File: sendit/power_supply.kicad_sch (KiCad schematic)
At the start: 44 parts, among them J36 Conn_01x02, J37 Conn_01x02, J38 JUMPER, U10 TPS61040DBV, U11 AP63205WU, U9 TPS7A2033PDBVR

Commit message: power system work and layout
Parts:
- removed C35: 22pF / 50v, Capacitor_SMD:C_0603_1608Metric, symbol Device:C_Small
- removed C38: 1uF / 50v, Capacitor_SMD:C_0603_1608Metric, symbol Device:C_Small
- removed D19: MBR0530, Diode_SMD:D_SOD-123, symbol Diode:MBR0530
- removed FB3: BLM18AG121SN1D, Inductor_SMD:L_0603_1608Metric, symbol Device:FerriteBead_Small
- removed U10: TPS61040DBV, Package_TO_SOT_SMD:SOT-23-5, symbol Regulator_Switching:TPS61040DBV
- added D20: SS36, Diode_SMD:D_SMA, symbol Diode:SS36
- added U10: MT3608, Package_TO_SOT_SMD:SOT-23-6, symbol Regulator_Switching:MT3608
- C30: value 10uF / 10v -> 22uF / 10v; LCSC C19702 -> (none)
- C35: renamed from C36; value 1uF / 50v -> 22uF / 50v
- L1: footprint Inductor_SMD:L_APV_ANR252012 -> Inductor_SMD:L_TechFuse_SL0630; LCSC C5832376 -> C167223
- R53: value 1.87M -> 390K 1%; LCSC C61679 -> (none)
- R54: value 100k -> 10k 0.1%; LCSC C25803 -> (none)
- renumbered C37 to C36, C39 to C37, C40 to C38, D20 to D19, J36 to J37, J37 to J38, J38 to J39, TP17 to TP15, TP15 to TP16, TP16 to TP17
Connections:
- net +24V: now also F7.1
- net +3.3V: now also JP1.3 (B); no longer JP1.1 (A)
- net +3.3VADC: now also TP16.1
- net +5V: now also U10.4 (EN), U10.5 (IN)
- net GND: now also U10.2 (GND)
- net VEXT: now also TP15.1
- net at C31.1, C32.1, C33.1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: now also JP1.1 (A); no longer JP1.3 (B), TP16.1
- net at C35.1: now also F7.2, R53.1, D20.1 (K); no longer F7.1
- net at R53.2, R54.1: now also U10.3 (FB)
- net at L1.2: now also D20.2 (A), U10.1 (SW)
- net at C34.1, F6.2, U11.2 (EN)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: no longer TP15.1
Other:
- note added: "POWER TOPOLOGY"
- moved on the sheet: C30, C35, C37, D15, D21, F7, JP1, L1, R51, R53, R54, R55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

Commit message: big change removing the usb hub and serial chip.
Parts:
- removed D16: MBR0530, Diode_SMD:D_SOD-123, symbol Diode:MBR0530
- removed J38: Conn_01x02, Connector_PinSocket_2.54mm:PinSocket_1x02_P2.54mm_Vertical, symbol Connector_Generic:Conn_01x02
- removed J39: JUMPER, symbol Connector_Generic:Conn_01x02
- added D17: SS36, Diode_SMD:D_SMA, symbol Diode:SS36
- renumbered C28 to C20, C29 to C21, C30 to C22, C31 to C23, C32 to C24, C33 to C25, C34 to C26, C35 to C27, C36 to C28, C37 to C29, C38 to C30, D17 to D16, J37 to J38, R51 to R45, R52 to R46, R53 to R47, R54 to R48, R55 to R49, TP14 to TP16, TP15 to TP17, TP16 to TP18, TP17 to TP19, TP18 to TP20, U9 to U7, U10 to U8, U11 to U9
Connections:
- net VEXT: now also F6.1, D17.1 (K)
- net at INPUT6.1 (Pin_1): now also D17.2 (A)
- no-connect marks 4 -> 2
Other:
- moved on the sheet: D18, INPUT6, J38, R46, TP17

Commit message: first pass fully routed.
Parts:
- added D20: GREEN, LED_SMD:LED_0603_1608Metric, symbol Device:LED
- added R46: 5.1k, Resistor_SMD:R_0603_1608Metric, symbol Device:R_Small_US
- renumbered D15 to D14, D16 to D15, D17 to D16, D18 to D17, D19 to D18, D20 to D19, R45 to R44, R46 to R45, TP20 to TP21
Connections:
- net +3.3VADC: now also D20.2 (A)
- net GND: now also R46.2
- new net: D20.1 (K), R46.1
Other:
- moved on the sheet: TP18

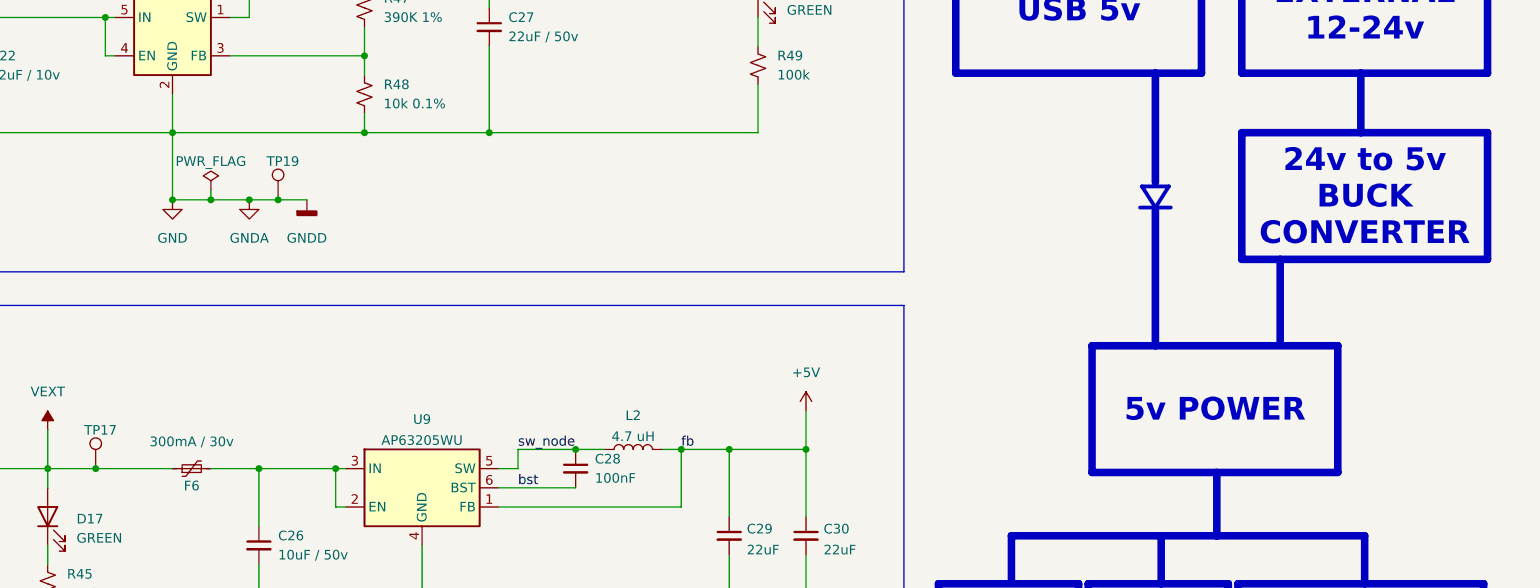
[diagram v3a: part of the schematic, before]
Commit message: beefed up the 24v to 5v circuit
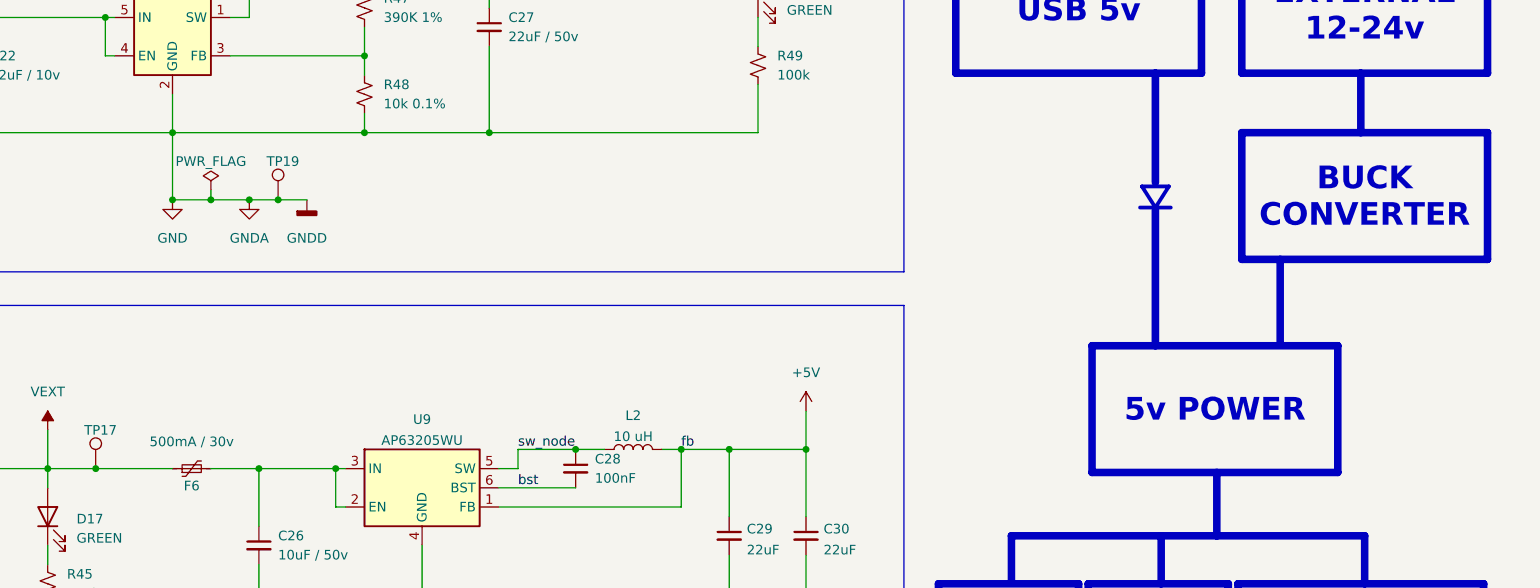
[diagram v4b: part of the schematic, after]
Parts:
- F6: value 300mA / 30v -> 500mA / 30v; footprint Fuse:Fuse_0805_2012Metric -> Fuse:Fuse_1206_3216Metric; LCSC C22378359 -> C455450
- L2: value 4.7 uH -> 10 uH; footprint Inductor_SMD:L_Neosid_SMS-ME3010 -> Inductor_SMD:L_Chilisin_BMRA00050530; LCSC C354557 -> C177248; PARTNUM CKCS3012-4.7uH/M -> FXL0530-100-M
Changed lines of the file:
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@@
 		)
 	)
-	(text_box "24v to 5v BUCK CONVERTER"
+	(text_box "BUCK CONVERTER"
 		(exclude_from_sim no)
 		(at 249.428 62.23 0)
@@
 			)
 		)
-		(property "Value" "4.7 uH"
+		(property "Value" "10 uH"
 			(at 168.91 102.4406 90)
 			(effects
@@
 			)
 		)
-		(property "Footprint" "Inductor_SMD:L_Neosid_SMS-ME3010"
+		(property "Footprint" "Inductor_SMD:L_Chilisin_BMRA00050530"
 			(at 168.91 104.14 0)
 			(effects
@@
 			)
 		)
-		(property "LCSC" "C354557"
+		(property "LCSC" "C177248"
 			(at 168.91 104.14 0)
 			(effects
@@
 			)
 		)
-		(property "PARTNUM" "CKCS3012-4.7uH/M"
+		(property "PARTNUM" "FXL0530-100-M"
 			(at 168.91 104.14 0)
 			(effects
@@
 			)
 		)
-		(property "Value" "300mA / 30v"
+		(property "Value" "500mA / 30v"
 			(at 110.49 103.124 90)
 			(effects
@@
 			)
 		)
-		(property "Footprint" "Fuse:Fuse_0805_2012Metric"
+		(property "Footprint" "Fuse:Fuse_1206_3216Metric"
 			(at 115.57 105.41 0)
 			(effects
@@
 			)
 		)
-		(property "LCSC" "C22378359"
+		(property "LCSC" "C455450"
 			(at 110.49 106.68 90)
 			(effects

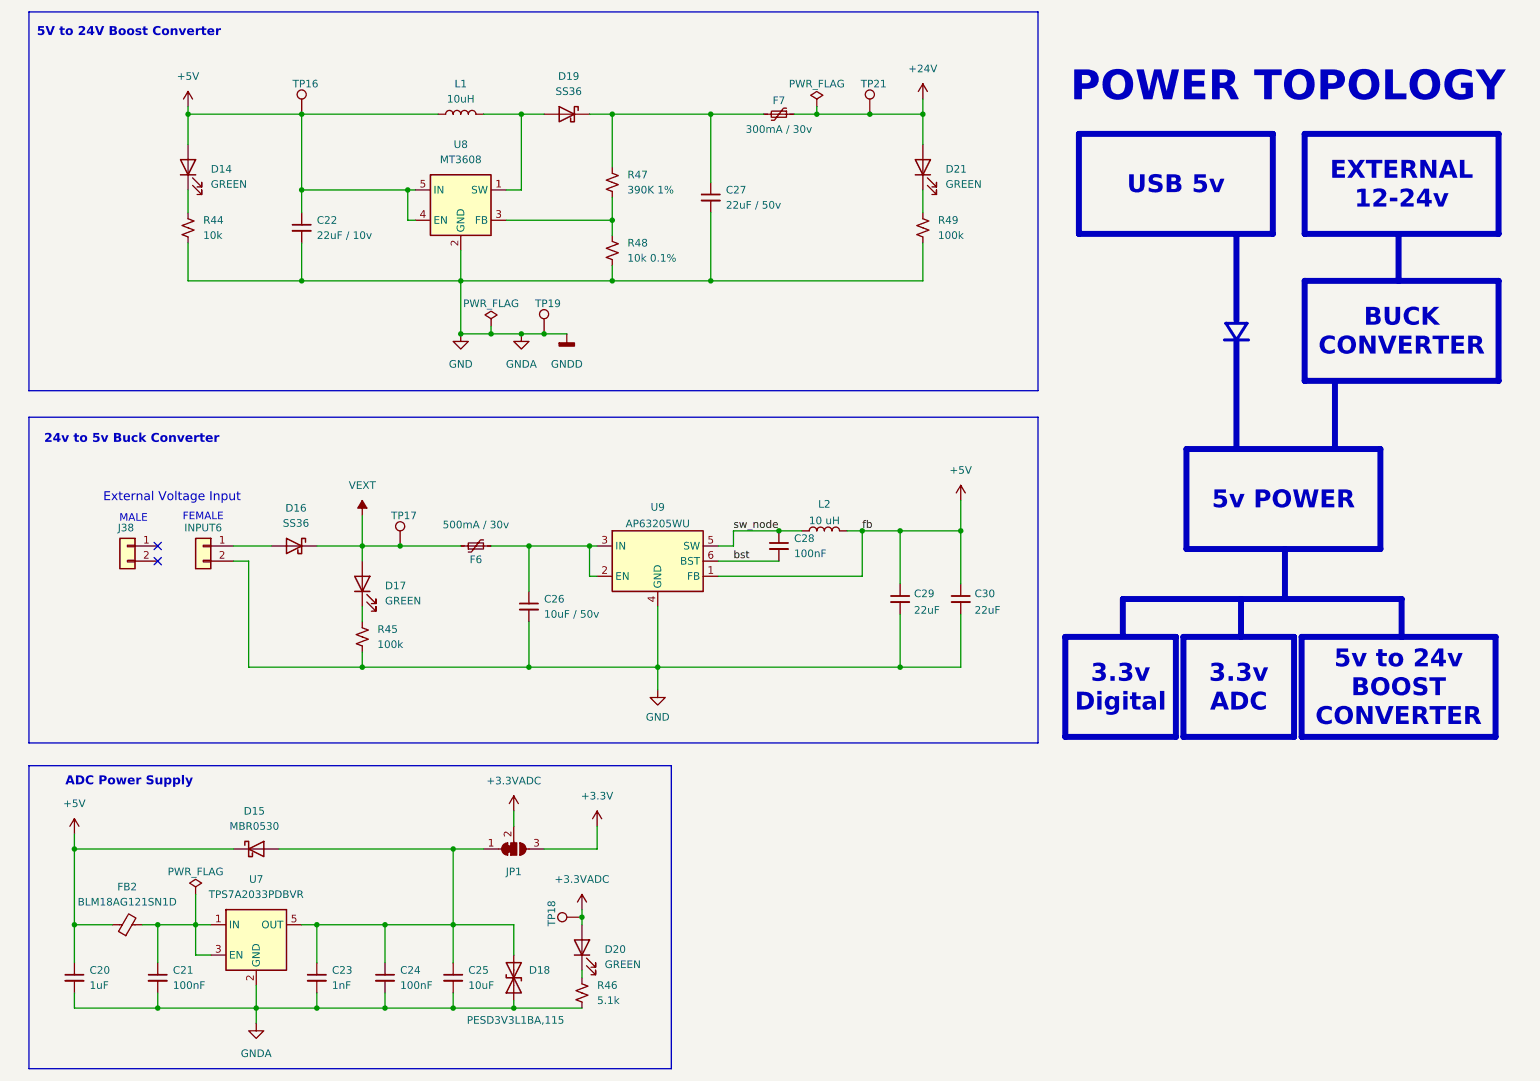
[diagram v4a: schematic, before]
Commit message: fixed erc errors
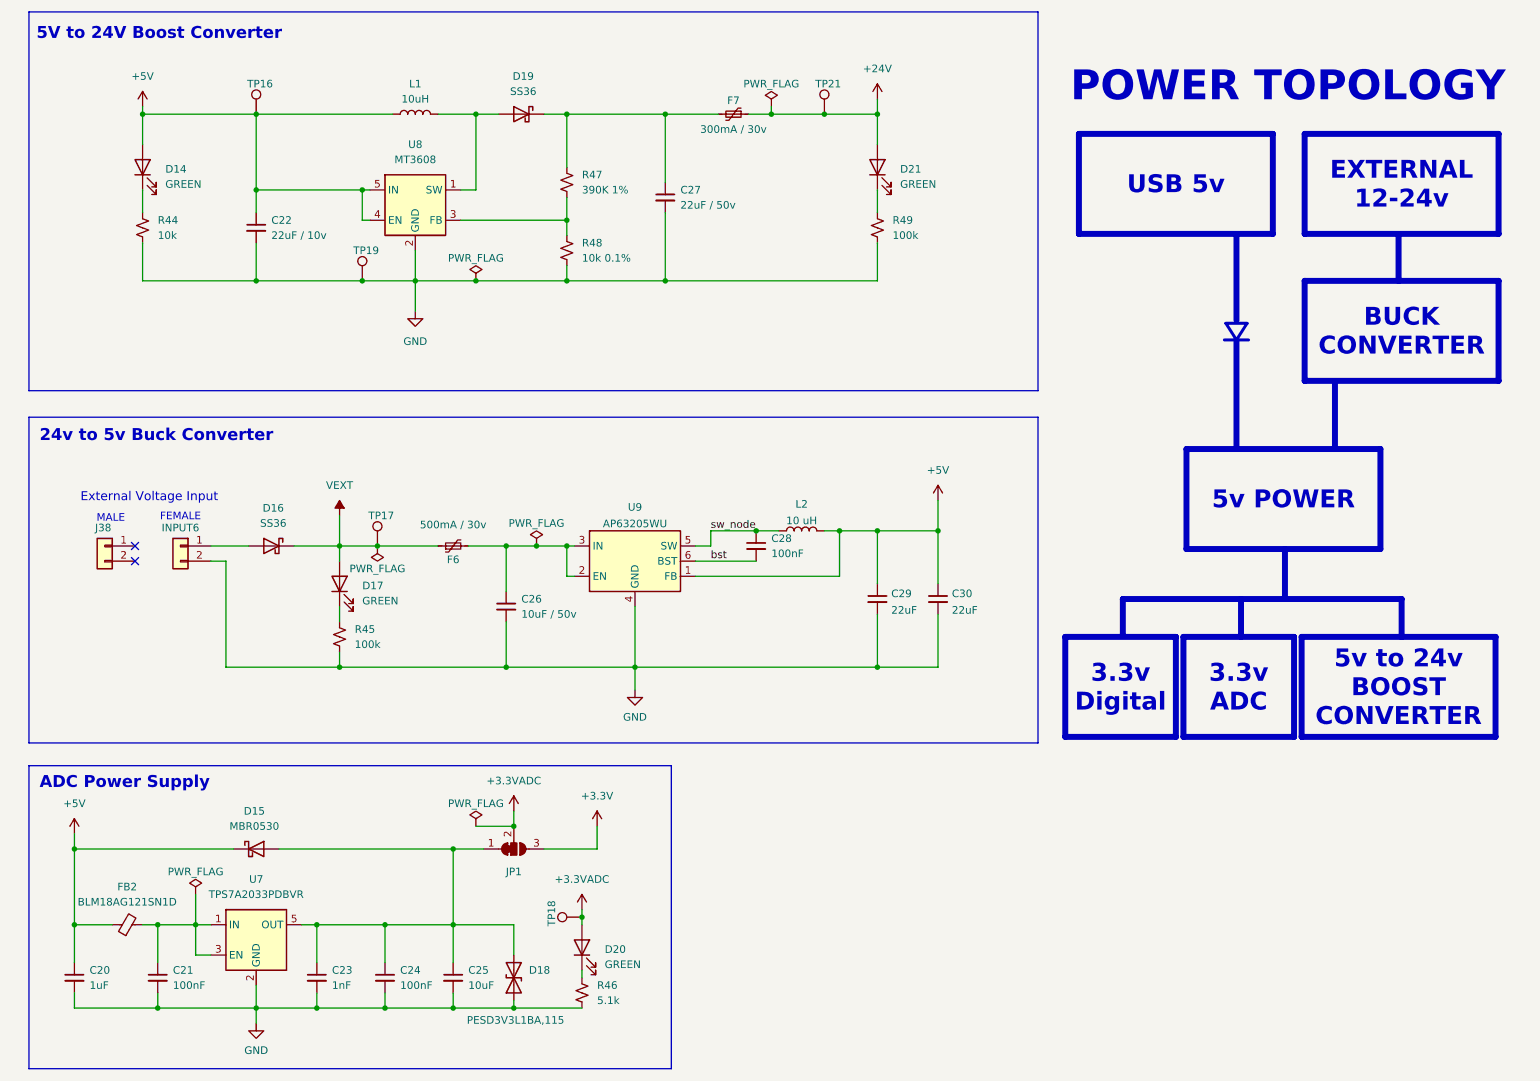
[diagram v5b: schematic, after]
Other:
- moved on the sheet: C22, C26, C27, C28, C29, C30, D14, D16, D17, D19, D21, F6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

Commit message: double checked power supplies + gave esp32-s3 proper voltage/ground symbols
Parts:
- L2: value 10 uH -> 4.7 uH; LCSC C177248 -> C177246; PARTNUM FXL0530-100-M -> FXL0530-4R7-M
- U8: LCSC (none) -> C84817
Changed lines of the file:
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@@
+			)
+		)
+		(property "LCSC" "C84817"
+			(at 100.33 49.53 0)
+			(effects
+				(font
+					(size 1.27 1.27)
+				)
+				(hide yes)
 			)
 		)
@@
 			)
 		)
-		(property "Value" "10 uH"
+		(property "Value" "4.7 uH"
 			(at 165.1 102.4406 90)
 			(effects
@@
 			)
 		)
-		(property "LCSC" "C177248"
+		(property "LCSC" "C177246"
 			(at 165.1 104.14 0)
 			(effects
@@
 			)
 		)
-		(property "PARTNUM" "FXL0530-100-M"
+		(property "PARTNUM" "FXL0530-4R7-M"
 			(at 165.1 104.14 0)
 			(effects

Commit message: moved the dc buck circuit away from the usb port.
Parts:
- U8: Rotation Offset (none) -> 90
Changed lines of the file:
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@@
+			)
+		)
+		(property "Rotation Offset" "90"
+			(at 100.33 49.53 0)
+			(effects
+				(font
+					(size 1.27 1.27)
+				)
+				(hide yes)
 			)
 		)

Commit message: some bom work
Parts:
- C22: value 22uF / 10v -> 22uF; LCSC (none) -> C84419
- C26: value 10uF / 50v -> 10uF / 35v
- C27: value 22uF / 50v -> 22uF / 35v; footprint Capacitor_SMD:C_0603_1608Metric -> Capacitor_SMD:C_0805_2012Metric; LCSC C15849 -> (none)
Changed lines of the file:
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@@
 			)
 		)
-		(property "Value" "22uF / 50v"
+		(property "Value" "22uF / 35v"
 			(at 144.78 49.5362 0)
 			(effects
@@
 			)
 		)
-		(property "Footprint" "Capacitor_SMD:C_0603_1608Metric"
+		(property "Footprint" "Capacitor_SMD:C_0805_2012Metric"
 			(at 142.24 48.26 0)
 			(effects
@@
 			)
 		)
-		(property "LCSC" "C15849"
+		(property "LCSC" ""
 			(at 142.24 48.26 0)
 			(effects
@@
 			)
 		)
-		(property "Value" "10uF / 50v"
+		(property "Value" "10uF / 35v"
 			(at 118.11 118.1162 0)
 			(effects
@@
 			)
 		)
-		(property "Value" "22uF / 10v"
+		(property "Value" "22uF"
 			(at 76.2 54.6162 0)
 			(effects
@@
 			)
 		)
-		(property "LCSC" ""
+		(property "LCSC" "C84419"
 			(at 73.66 53.34 0)
 			(effects
